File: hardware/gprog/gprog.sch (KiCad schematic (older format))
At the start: 27 parts, among them IC1 ATMEGA48P, P1 ISP x2560, P2 USB, P3 ISP x48, U1 74HC125, X1 12MHz

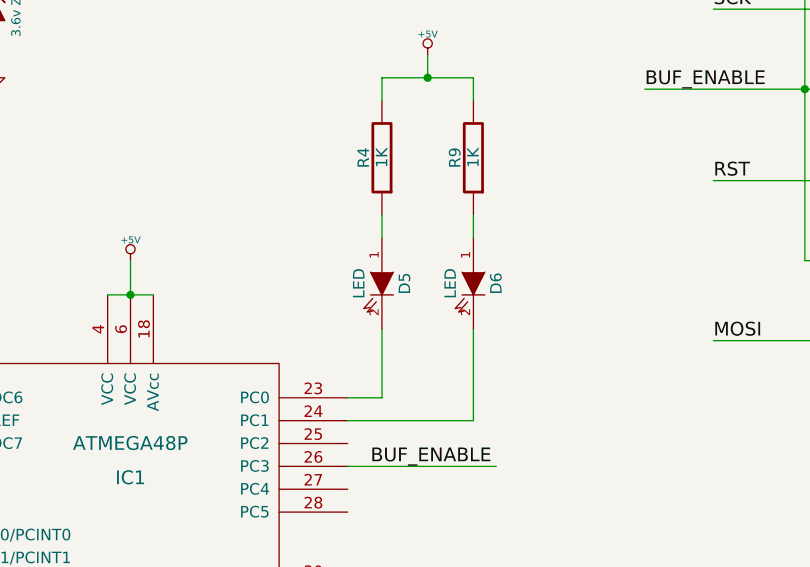
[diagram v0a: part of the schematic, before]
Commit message: GPROG: Minor changes to board layout. BOM completed for element14. DigiKey        parts not completed.
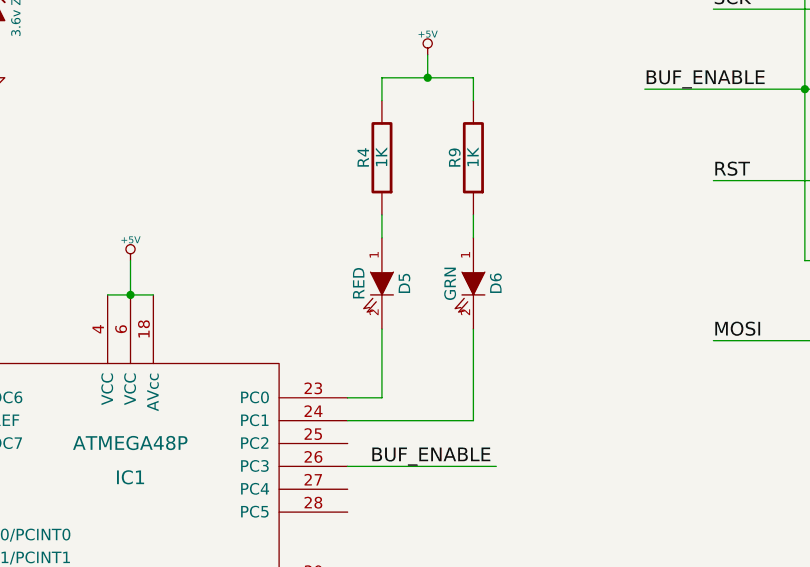
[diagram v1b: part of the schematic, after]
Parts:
- D5: value LED -> RED
- D6: value LED -> GRN
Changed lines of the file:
@@
-EESchema Schematic File Version 2  date 14/12/2011 10:47:55 a.m.
+EESchema Schematic File Version 2  date 15/12/2011 12:23:25 p.m.
 LIBS:power
 LIBS:device
@@
 Sheet 1 1
 Title "G9X USB Programmer"
-Date "13 dec 2011"
+Date "14 dec 2011"
 Rev "1.0"
 Comp ""
@@
 P 5700 4050
 F 0 "D6" H 5700 4150 50  0000 C CNN
-F 1 "LED" H 5700 3950 50  0000 C CNN
+F 1 "GRN" H 5700 3950 50  0000 C CNN
 	1    5700 4050
 	0    1    1    0
@@
 P 5300 4050
 F 0 "D5" H 5300 4150 50  0000 C CNN
-F 1 "LED" H 5300 3950 50  0000 C CNN
+F 1 "RED" H 5300 3950 50  0000 C CNN
 	1    5300 4050
 	0    1    1    0

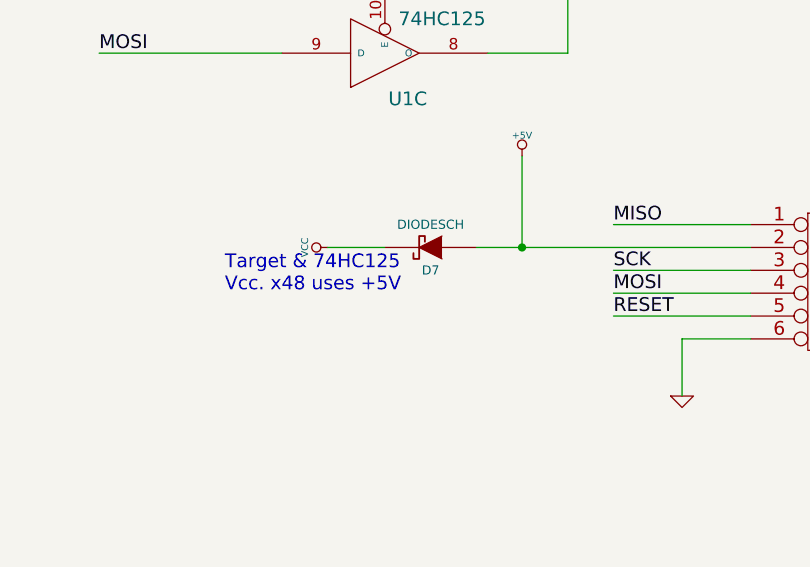
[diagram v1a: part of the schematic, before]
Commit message: gPROG: Had to revert USB Manufacturer(Vendor) Name back so that AVRDUDE will recognise us as a USBasp
PCB -- added a big, fat "+" symbol to pin 1 of the USB pin header.
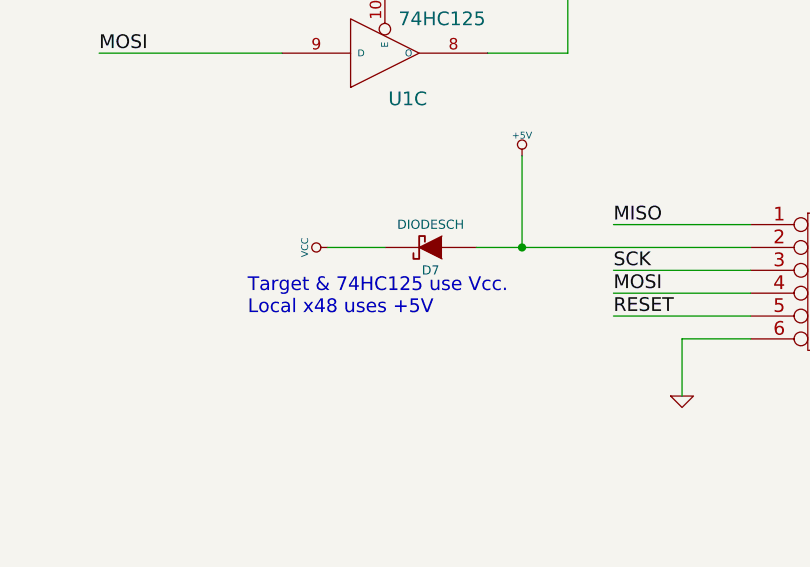
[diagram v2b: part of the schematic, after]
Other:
- note added: "Target & 74HC125 use Vcc. \nLocal x48 uses +5V"
- note removed: "Target & 74HC125 \nVcc. x48 uses +5V"
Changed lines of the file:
@@
-EESchema Schematic File Version 2  date 15/12/2011 12:23:25 p.m.
+EESchema Schematic File Version 2  date 26/01/2012 11:43:36 a.m.
 LIBS:power
 LIBS:device
@@
 Sheet 1 1
 Title "G9X USB Programmer"
-Date "14 dec 2011"
-Rev "1.0"
+Date "25 jan 2012"
+Rev "1.1"
 Comp ""
 Comment1 "Customised for G9X by JWB. Converted ro KiCAD by Gruvin"
@@
 	1    0    0    -1
 $EndComp
-Text Notes 7300 5350 0    60   ~ 0
-Target & 74HC125 \nVcc. x48 uses +5V
+Text Notes 7400 5450 0    60   ~ 0
+Target & 74HC125 use Vcc. \nLocal x48 uses +5V
 Wire Wire Line
 	8000 5150 7750 5150

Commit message: gprog schematic, PCB & firmware updated to v1.2 -- final release candidate 2
This is the version with the fixes to the moumental screw-ups made 
by myself, as discovered 2012-01-29. This should now be the final
prodcution version.
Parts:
- U1: value 74HC125 -> 74HC126; symbol 74LS125 -> 74LS126
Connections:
- wire segments 101 -> 100
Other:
- note added: "Target & 74HC126 use Vcc. \nLocal x48 uses +5V"
- note removed: "Target & 74HC125 use Vcc. \nLocal x48 uses +5V"
- moved on the sheet: R8

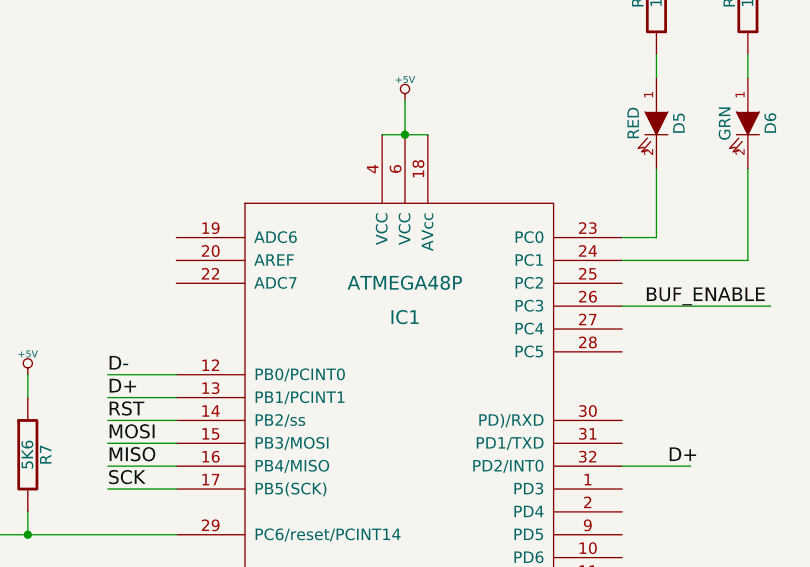
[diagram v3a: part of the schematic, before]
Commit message: gprog: pre-production last(?) minute checks. Reduced some over-sized holes. Changed part value of MCU to ATMEGA88P (instead of '48P)
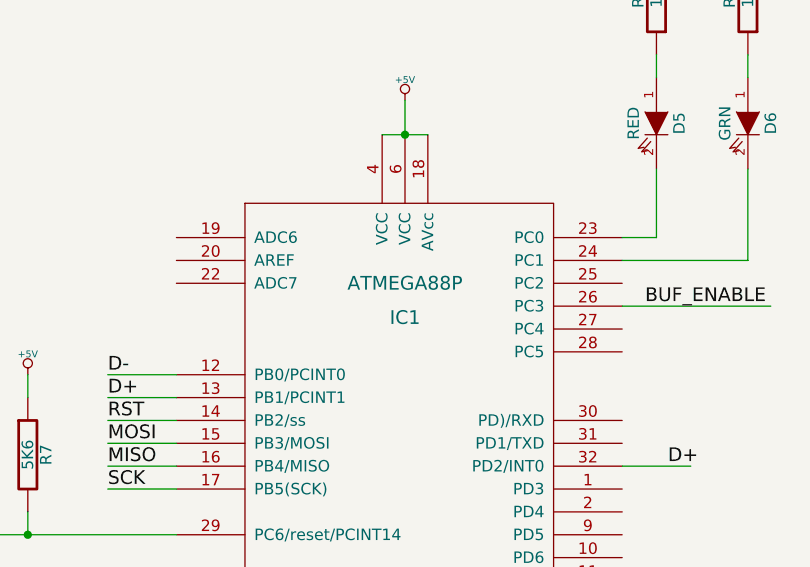
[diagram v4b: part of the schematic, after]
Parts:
- IC1: value ATMEGA48P -> ATMEGA88P
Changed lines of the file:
@@
-EESchema Schematic File Version 2  date 29/01/2012 10:48:34 p.m.
+EESchema Schematic File Version 2  date 1/02/2012 11:24:37 p.m.
 LIBS:power
 LIBS:device
@@
 Sheet 1 1
 Title "G9X USB Programmer"
-Date "29 jan 2012"
+Date "1 feb 2012"
 Rev "1.2"
 Comp ""
@@
 P 4200 5350
 F 0 "IC1" H 4200 5800 60  0000 C CNN
-F 1 "ATMEGA48P" H 4200 5950 60  0000 C CNN
+F 1 "ATMEGA88P" H 4200 5950 60  0000 C CNN
 	1    4200 5350
 	1    0    0    -1

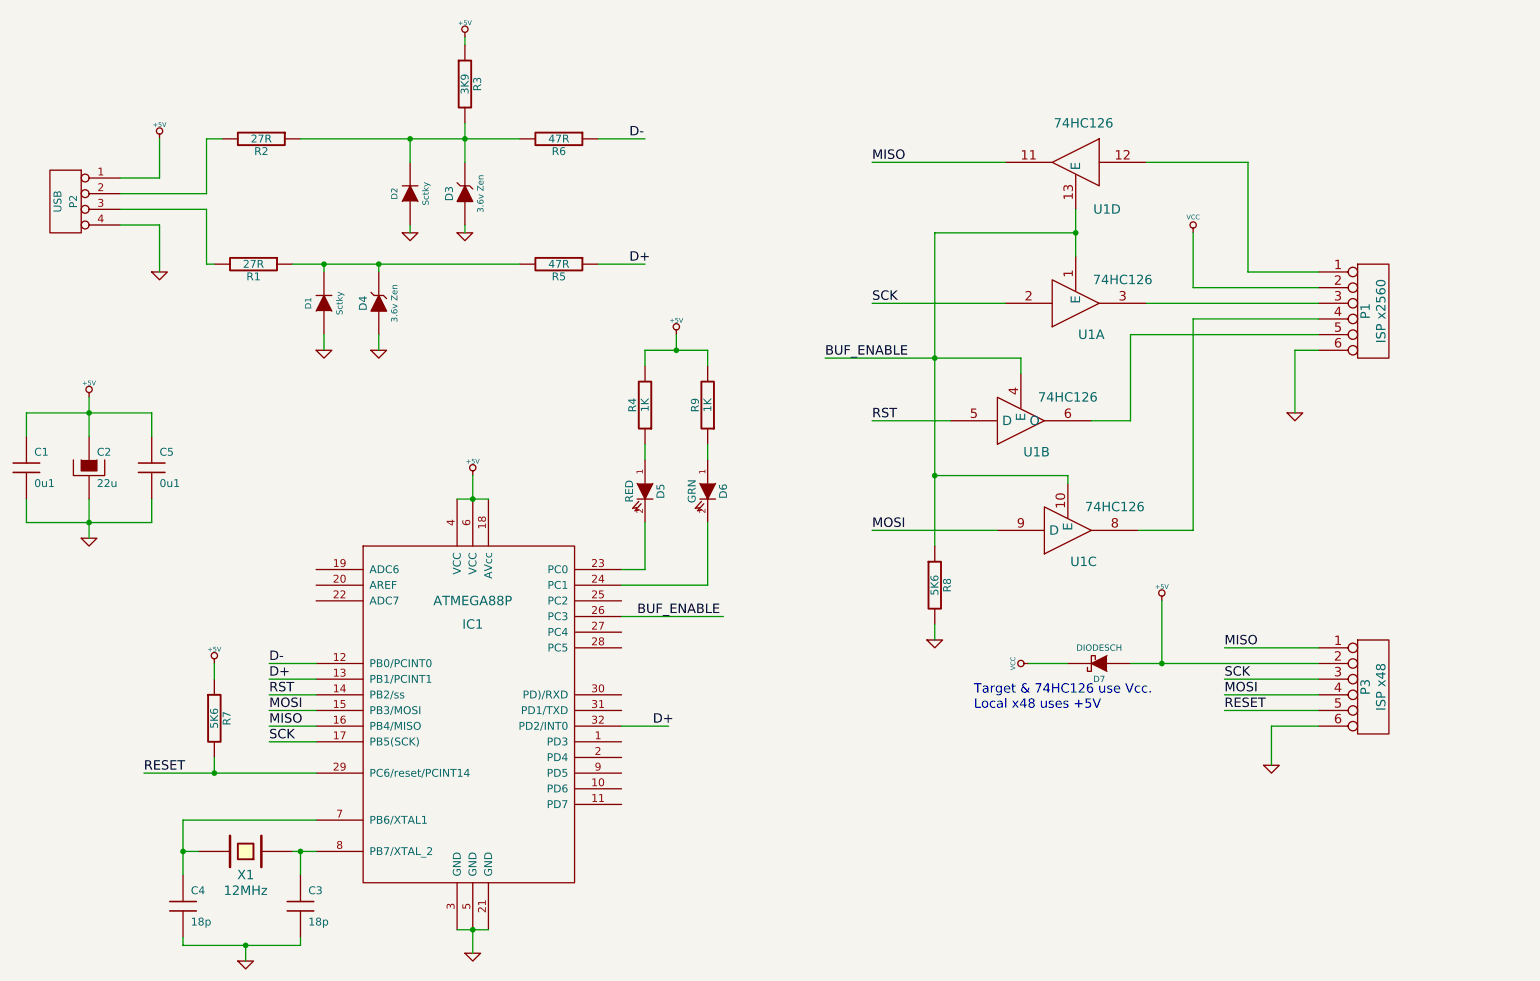
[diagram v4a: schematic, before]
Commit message: Mainly gProg v4.2 updated ready for Chinese factory quoting. (Frozen.)
Also added files on my local machine not in repository, that should be.
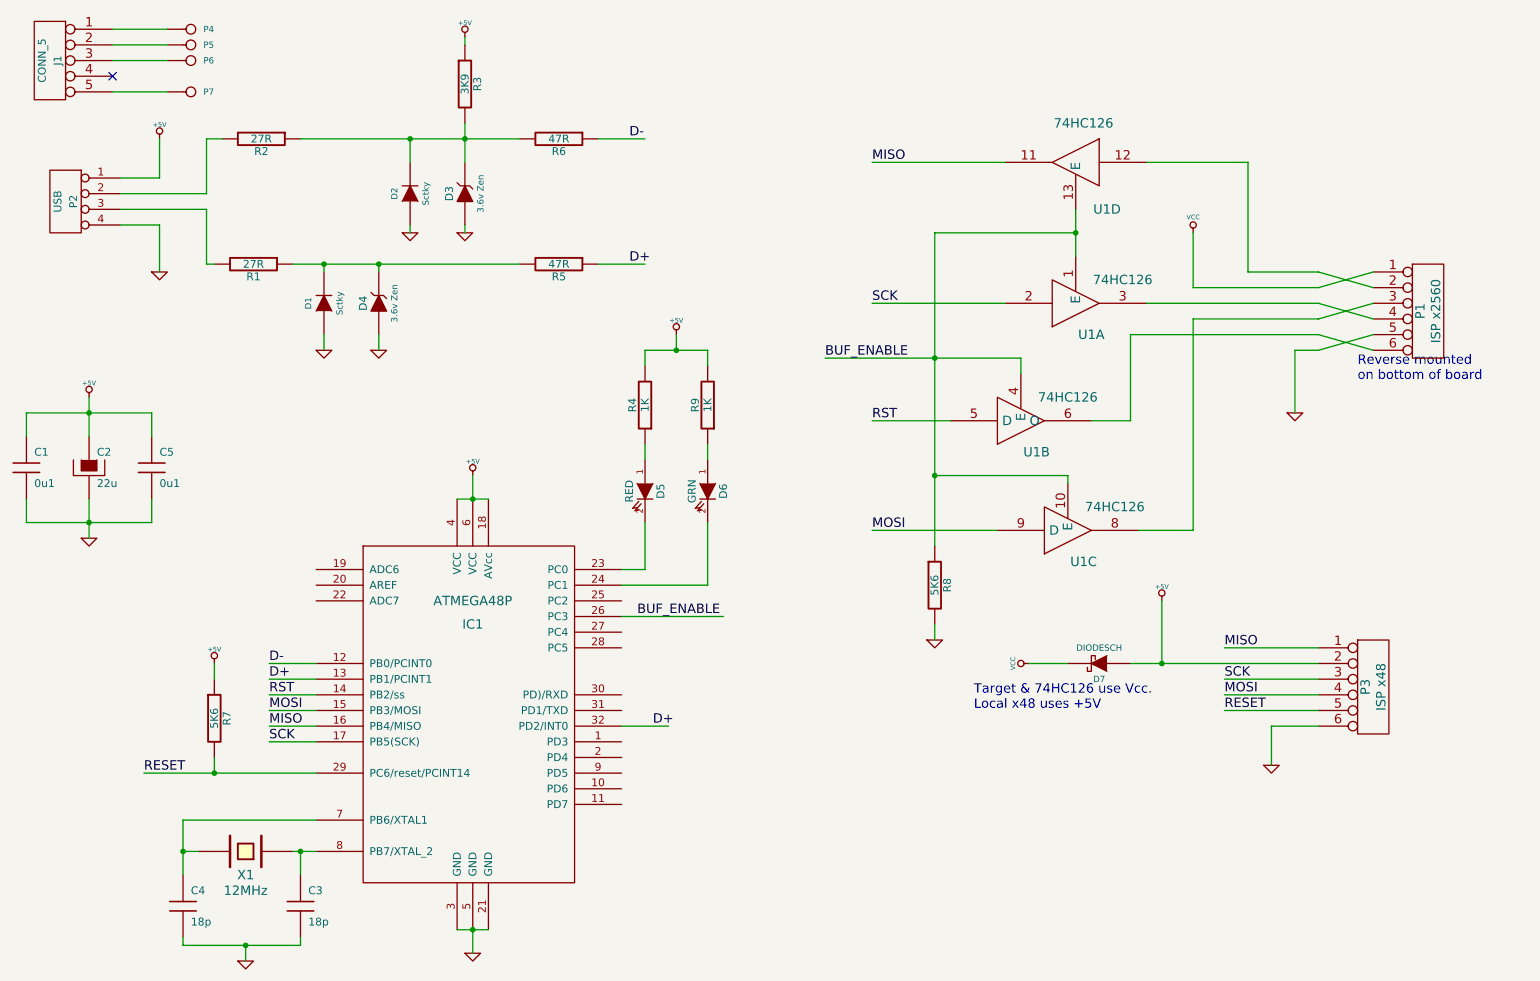
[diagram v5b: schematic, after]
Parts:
- added J1: CONN_5, symbol CONN_5
- added P4, P5, P6, P7: CONN_1, symbol CONN_1
- IC1: value ATMEGA88P -> ATMEGA48P
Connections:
- wire segments 100 -> 110
- no-connect marks 0 -> 1
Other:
- note added: "Reverse mounted\non bottom of board"
- moved on the sheet: P1
